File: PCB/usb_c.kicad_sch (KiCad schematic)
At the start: 4 parts

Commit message: task: alert on Basic-library alternatives during JLC part matching (#33)
* task: alert on Basic-library alternatives during JLC part matching

JLC's "Extended" library carries a per-unique-part setup fee on top of
unit price; "Basic" doesn't. That fee doesn't amortize well on a board
with many distinct low-quantity parts -- confirmed the hard way: our
first real JLCPCB assembly quote came back at $333.84 vs PCBWay's
~$190 for the same order, and all 33 of our matched parts were
Extended.

jlc_match.py now does a secondary search for a same-value/same-package
Basic-library part whenever the real match lands on Extended, and
flags it in the report (new BasicAlt column + a Status alert) rather
than silently leaving it. On the current board this surfaces 11
plausible Basic-library swaps (common resistor/cap values, and the
generic 1N4148W diode and 2N7002 MOSFET, which are industry-standard
parts many brands stock identically).

This is alert-only, same as the rest of this script -- it doesn't
touch the schematic. Spot-checked 4 of the 11 suggestions directly
against JLC's catalog to confirm value/package actually match, not
just a keyword hit.

Co-Authored-By: Claude Sonnet 5 <noreply@anthropic.com>

* fix: two correctness bugs in Basic-library alternative matching

1. find_basic_alternative() trusted the raw keyword-search hit without
   verifying the candidate's actual value -- JLC's fuzzy full-text search
   can return a wrong-value part that just shares digits (e.g. searching
   "100 0402" surfaced a 1kΩ resistor, EIA code "1001", as a false match
   for a 100Ω part). Now parses and compares the actual numeric value
   (with unit) before accepting a candidate; falls back to exact
   model-name matching for non-numeric values (generic diode/transistor
   part families like "1N4148W", "2N7002").

2. The new value parser's regex required the unit to be the first
   character of the string, but JLC resistor descriptions carry a
   Chinese prefix ("厚膜电阻 10kΩ ±1%" = "thi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
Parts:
- R_CC1, R_CC2: LCSC C105872 -> C25905; MF Yageo -> UNI-ROYAL(Uniroyal Elec); Manufacturer_Part_Number RC0402FR-075K1L -> 0402WGF5101TCE
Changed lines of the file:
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@@
 			)
 		)
-		(property "MF" "Yageo"
+		(property "MF" "UNI-ROYAL(Uniroyal Elec)"
 			(at 0 0 0)
 			(hide yes)
@@
 			)
 		)
-		(property "Manufacturer_Part_Number" "RC0402FR-075K1L"
+		(property "Manufacturer_Part_Number" "0402WGF5101TCE"
 			(at 0 0 0)
 			(hide yes)
@@
 			)
 		)
-		(property "LCSC" "C105872"
+		(property "LCSC" "C25905"
 			(at 0 0 0)
 			(hide yes)
@@
 			)
 		)
-		(property "MF" "Yageo"
+		(property "MF" "UNI-ROYAL(Uniroyal Elec)"
 			(at 0 0 0)
 			(hide yes)
@@
 			)
 		)
-		(property "Manufacturer_Part_Number" "RC0402FR-075K1L"
+		(property "Manufacturer_Part_Number" "0402WGF5101TCE"
 			(at 0 0 0)
 			(hide yes)
@@
 			)
 		)
-		(property "LCSC" "C105872"
+		(property "LCSC" "C25905"
 			(at 0 0 0)
 			(hide yes)

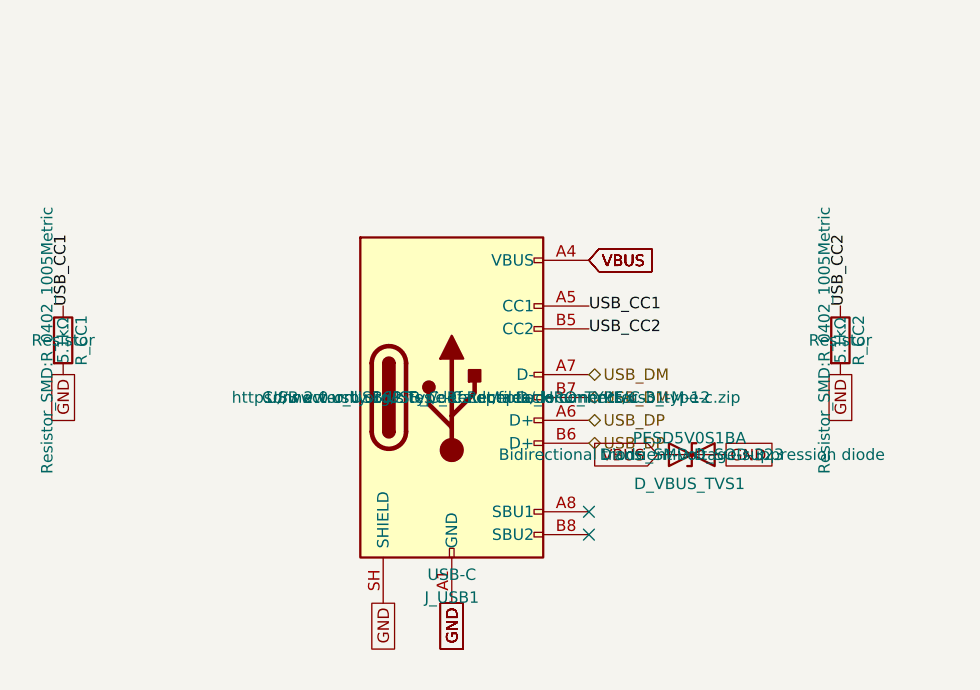
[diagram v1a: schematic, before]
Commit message: fix: make every BOM Value unambiguous for the fab, and switch D_INV_ISO1 to SOT-323 (#61)
* fix: make every BOM Value unambiguous for the fab, and switch D_INV_ISO1 to SOT-323

PCBWay flagged D_INV_ISO1: "BAT54W" is SOT-323 from nearly every maker, but we
had picked Yangjie's SOD-123 variant. A fab only sees Designator, Footprint,
Quantity and Value in the BOM (never MF/MPN/LCSC), so a bare part name is
ambiguous. Fixes the class of problem, not just this part:

- Every component's Value is now "<label> | <MPN> | <manufacturer> | <package>"
  (label dropped when it repeats the MPN; commas/periods stripped so the CSV
  never needs quoting). BT1 keeps its RIGHT-ANGLE HORIZONTAL note. Applied to
  all 81 parts across every sheet and the PCB.
- scripts/bom_values.py builds, applies, and checks these values, including
  that the PCB copy of Value/MF/MPN/footprint matches the schematic. New
  footprints must be added to its package table on purpose; hand-sourced parts
  with no MPN (J_STICK1) are listed explicitly.
- D_INV_ISO1 -> Diodes BAT54W-7-F in SOT-323 (common part, several makers).
  Pin 1 anode / pin 2 not connected / pin 3 cathode, confirmed against
  Nexperia's numbered pinning table and Diodes' datasheet. Uses KiCad's
  Diode:BAT54W symbol; PCB footprint replaced and rerouted. Electrically the
  same BAT54 family (30V, 200mA, 2uA leakage at 25V), so the SPICE model and
  scripts/spice/latch_sim.py still pass.
- Layout diagrams now say AO3401A for Q_PWR1 (they were stale since it was
  swapped from DMG2305UX) and BAT54W-7-F/SOT-323 for D_INV_ISO1.
- Repo CLAUDE.md documents the Value rule and the script.

ERC/DRC clean; production files regenerated.

Co-Authored-By: Claude Sonnet 5 <noreply@anthropic.com>

* chore: commit KiCad project settings (reordered used-designators list)

Co-Authored-By: Claude Sonnet 5 <noreply@anthropic.com>

---------

Co-authored-by: Claude Sonnet 5 <noreply@anthropic.com>
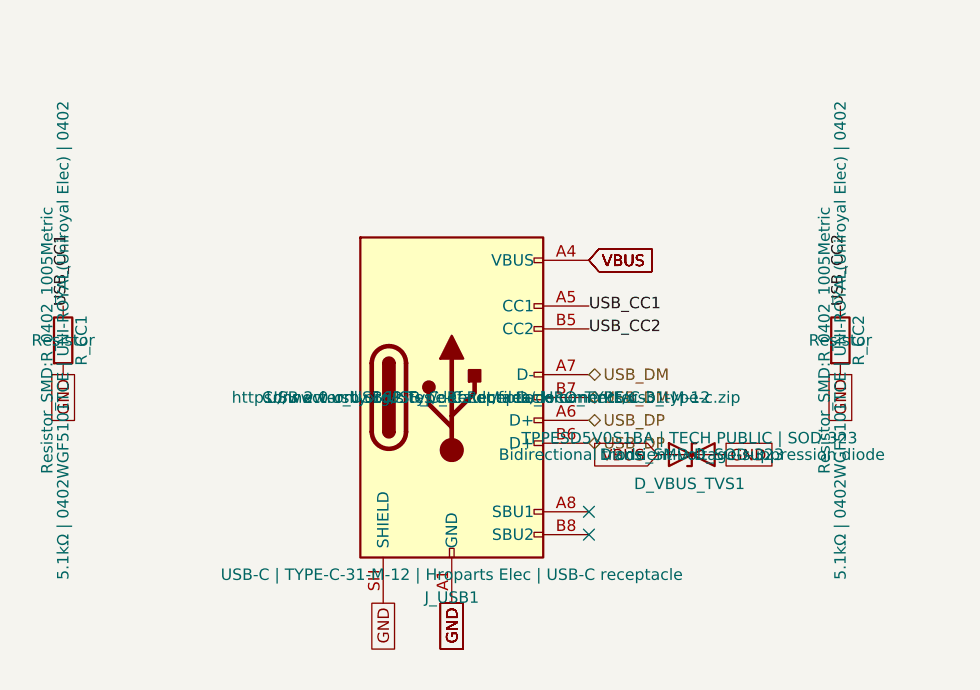
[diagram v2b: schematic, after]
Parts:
- D_VBUS_TVS1: value PESD5V0S1BA -> TPPESD5V0S1BA | TECH PUBLIC | SOD-323
- J_USB1: value USB-C -> USB-C | TYPE-C-31-M-12 | Hroparts Elec | USB-C receptacle
- R_CC1, R_CC2: value 5.1kΩ -> 5.1kΩ | 0402WGF5101TCE | UNI-ROYAL(Uniroyal Elec) | 0402
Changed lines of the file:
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@@
 			)
 		)
-		(property "Value" "USB-C"
+		(property "Value" "USB-C | TYPE-C-31-M-12 | Hroparts Elec | USB-C receptacle"
 			(at 148.59 127.635 0)
 			(show_name no)
@@
 			)
 		)
-		(property "Value" "5.1kΩ"
+		(property "Value" "5.1kΩ | 0402WGF5101TCE | UNI-ROYAL(Uniroyal Elec) | 0402"
 			(at 105.41 101.6 90)
 			(show_name no)
@@
 			)
 		)
-		(property "Value" "5.1kΩ"
+		(property "Value" "5.1kΩ | 0402WGF5101TCE | UNI-ROYAL(Uniroyal Elec) | 0402"
 			(at 191.77 101.6 90)
 			(show_name no)
@@
 			)
 		)
-		(property "Value" "PESD5V0S1BA"
+		(property "Value" "TPPESD5V0S1BA | TECH PUBLIC | SOD-323"
 			(at 175 112.46 0)
 			(show_name no)
